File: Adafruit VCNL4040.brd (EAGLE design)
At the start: 19.8 x 16.5 mm, 17 parts, among them Q2 BSS138, U1 VCNL4040M3OE, U2 AP2112K-3.3

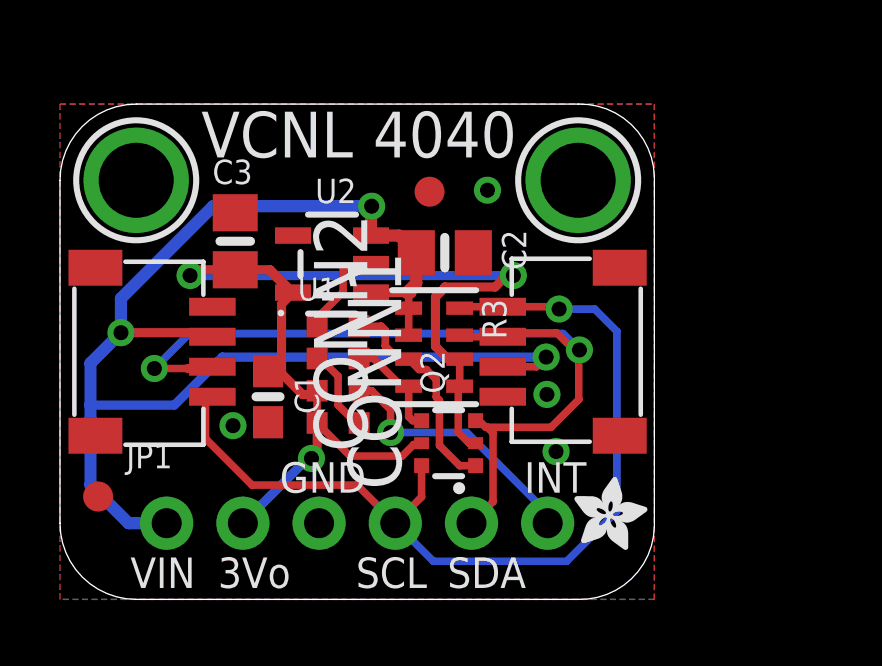
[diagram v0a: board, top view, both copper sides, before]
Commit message: setup with cookiecutter and latest pcb rev.
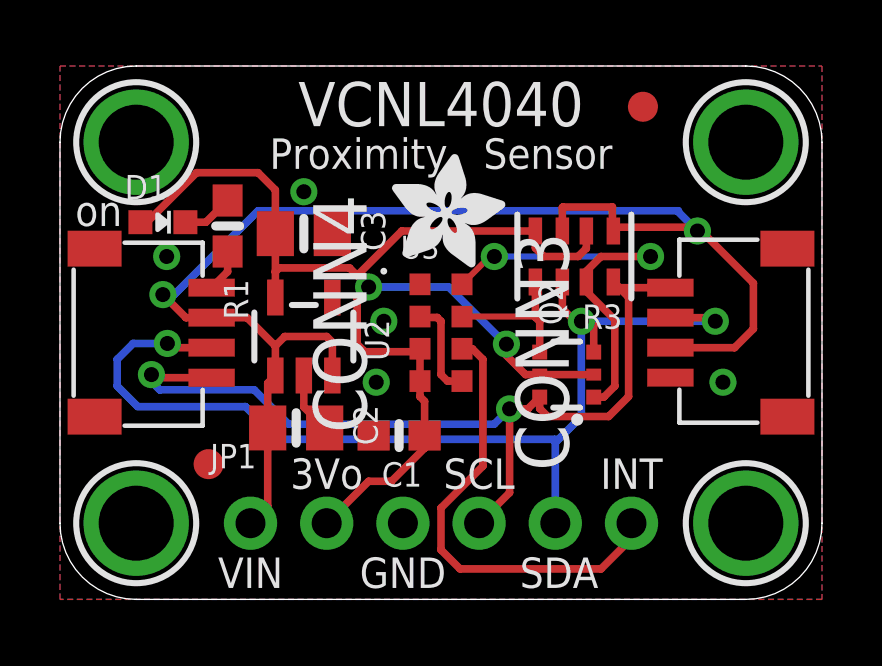
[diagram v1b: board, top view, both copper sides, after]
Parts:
- removed CONN1, CONN2: STEMMA_I2C_QT, microbuilder:JST_SH4
- removed FID1, FID2: FIDUCIAL_1MM, microbuilder:FIDUCIAL_1MM
- removed U$27: (no value), microbuilder:PCBFEAT-REV-040
- removed U$3, U$4: MOUNTINGHOLE2.5, microbuilder:MOUNTINGHOLE_2.5_PLATED
- removed U$8: (no value), microbuilder:ADAFRUIT_2.5MM
- removed U1: VCNL4040M3OE, VCNL4040M3OE:VISHAY_VCNL4040_4X2X1.1
- added CONN3, CONN4: STEMMA_I2C_QT, microbuilder:JST_SH4
- added D1: GREEN, microbuilder:CHIPLED_0603_NOOUTLINE
- added FID3, FID4: FIDUCIAL_1MM, microbuilder:FIDUCIAL_1MM
- added R1: 10K, microbuilder:0603-NO
- added U$17, U$19, U$21: MOUNTINGHOLE2.5, microbuilder:MOUNTINGHOLE_2.5_PLATED
- added U$22: (no value), microbuilder:ADAFRUIT_3.5MM
- added U$25: (no value), microbuilder:PCBFEAT-REV-040
- added U$30, U$31: (no value), silks:STEMMAQT
- added U3: VCNL4040M3OE, VCNL4040M3OE:VISHAY_VCNL4040_4X2X1.1
- U$1: value (none) -> MOUNTINGHOLE2.5; device microbuilder:ADAFRUIT_3.5MM -> microbuilder:MOUNTINGHOLE_2.5_PLATED
- moved C2 7.66 mm to (7.87, 5.71)
- moved U$1 7.12 mm to (2.54, 15.2), flipped to the top
- moved R3 5.57 mm to (17.1, 11.4), turned to 180 degrees
- moved C1 4.56 mm to (11.3, 5.46), turned to 180 degrees
- moved Q2 4.55 mm to (16.9, 7.49)
- moved JP1 2.79 mm to (12.7, 2.54)
- moved U2 2.59 mm to (8.13, 8.76), turned to 0 degrees
- moved C3 2.30 mm to (8.13, 12.2), turned to 0 degrees
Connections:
- removed net VIN: C2.1, CONN1.2, CONN2.2, JP1.1, R3.1, R3.2, U2.1, U2.3
- new net N$2: D1.C, R1.1
- new net VCC: C2.1, CONN3.2, CONN4.2, JP1.1, R3.1, R3.3, U2.1, U2.3
- net 3.3V: now also D1.A, R3.2, R3.4, U3.3, U3.4; no longer R3.5, R3.6, U1.3, U1.4
- net CATHODE: now also U3.2, U3.5; no longer U1.2, U1.5
- net GND: now also CONN3.1, CONN4.1, R1.2, U3.1; no longer CONN1.1, CONN2.1, U1.1
- net INT: now also U3.6; no longer U1.6
- net SCL: now also CONN3.4, CONN4.4; no longer CONN1.4, CONN2.4
- net SCL_3V: now also R3.7, U3.8; no longer R3.3, U1.8
- net SDA: now also CONN3.3, CONN4.3, R3.6; no longer CONN1.3, CONN2.3, R3.7
- net SDA_3V: now also R3.5, U3.7; no longer R3.4, U1.7
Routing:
- net VIN: track 47.1 -> 0.00 mm, vias 3 -> 0
- net VCC: track 0.00 -> 46.5 mm, vias 0 -> 2
- net SCL_3V: track 7.34 -> 14.1 mm, vias 0 -> 2
- net INT: track 8.75 -> 15.3 mm, vias 1 -> 0
- net SDA: track 30.3 -> 36.0 mm, vias 2 -> 3
- net 3.3V: track 40.1 -> 42.9 mm, vias 3 -> 2
- net N$2: track 0.00 -> 1.71 mm
- net SDA_3V: track 3.54 -> 4.85 mm
- net SCL: track 31.5 -> 30.2 mm, vias 1 -> 2
- net GND: track 3.31 -> 3.46 mm, vias 4 -> 5
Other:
- board size 19.8 x 16.5 mm -> 25.4 x 17.8 mm
- board text added: "Proximity & Ambient Light Sensor"
- board text added: "VCNL4040"
- board text added: "VLogic/Vcc: 3-5VDC I2C Address: 0x60"
- board text added: "on"
- board text removed: "4040"
- board text removed: "VCNL"
- board text removed: "by Kattni!"
